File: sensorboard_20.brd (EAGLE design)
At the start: 100 x 58 mm, 107 parts, among them IC1 ECMF02-2AMX6, IC2_ESP32S2WROOMM22S2 ESP32-S2-WROOM_M22S2H3200PH3Q0, IC4 TPA6211A1DRBR, J4_USB USB_CONN, J5_AUDIO SJ-3523-SMT-TR, J6_OAT 2.5mm JACK, J7 30310-6002HB, U1 LPS22HB, U10-MAG_SENSOR MMC5983MA, U11 LDL212PV33R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

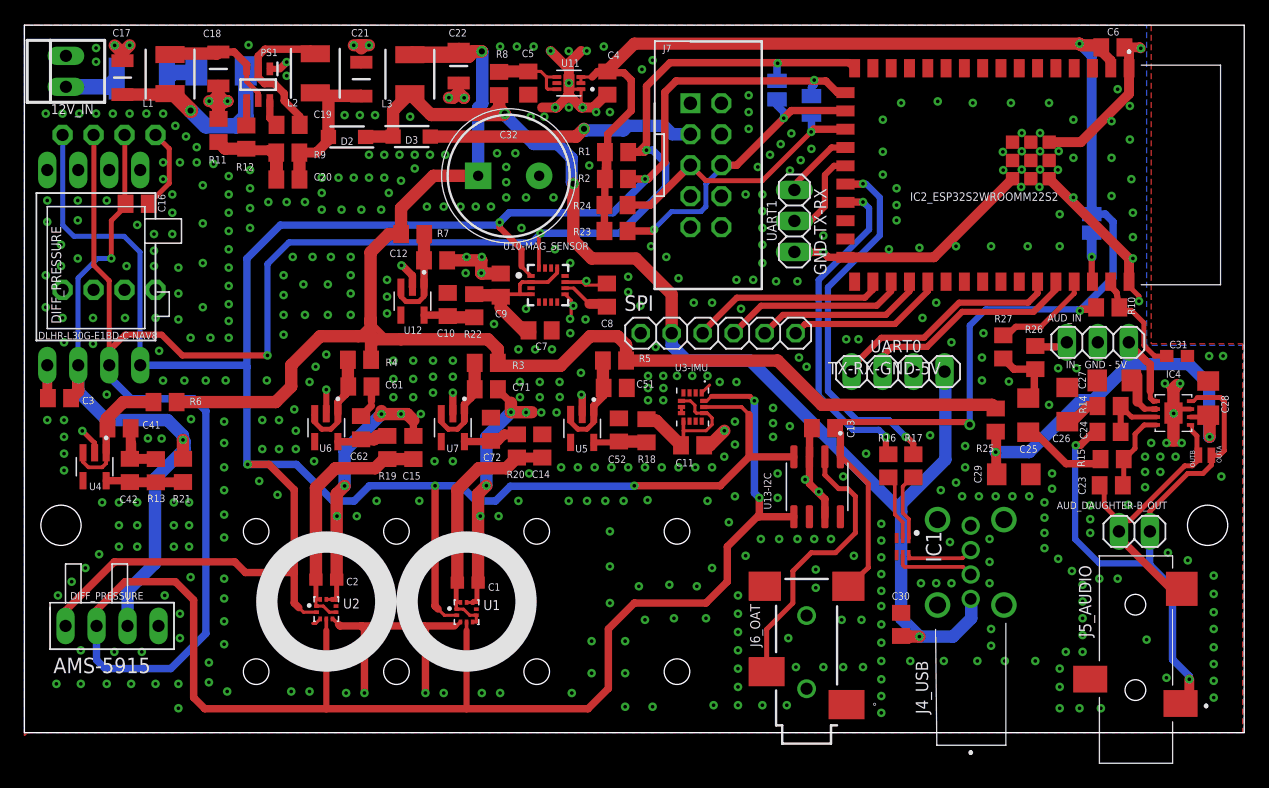
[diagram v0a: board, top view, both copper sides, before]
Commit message: Upload v20 files
Extend UART0 connector with EN, GPIO0 pins (Fixes #2)
Move ESP_AUD, WIFI_EN to different ESP32 pins (Fixes #3)
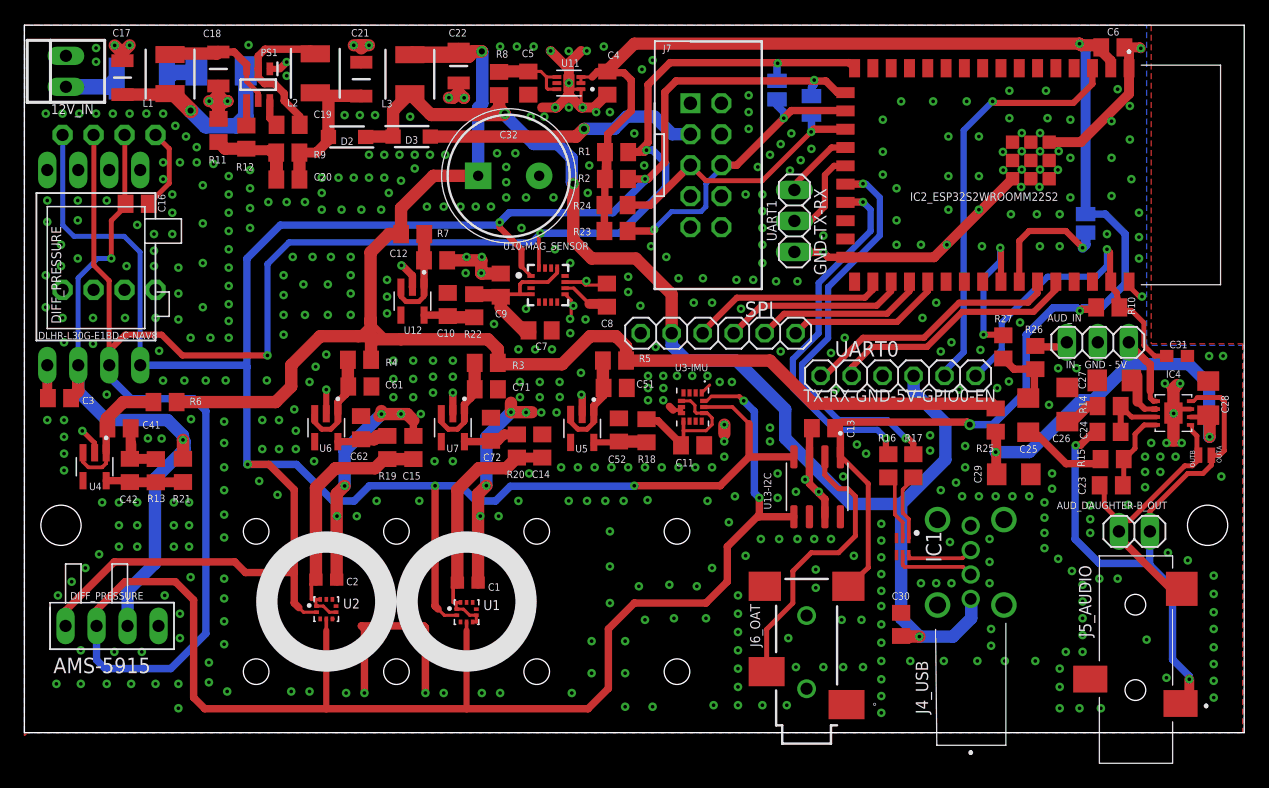
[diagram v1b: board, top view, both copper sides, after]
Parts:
- UART0: device pinhead:1X04 -> pinhead_dD:1X06
- moved WIFI_EN 0.50 mm to (87.0, 41.8)
- moved UART0 0.35 mm to (71.6, 29.2)
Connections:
- removed net N$7: C31.1, IC2_ESP32S2WROOMM22S2.41, R10.1
- new net EN: C31.1, IC2_ESP32S2WROOMM22S2.41, R10.1, UART0.6
- new net GPIO0: IC2_ESP32S2WROOMM22S2.3, UART0.5
- net ESP_AUD: now also IC2_ESP32S2WROOMM22S2.35; no longer IC2_ESP32S2WROOMM22S2.39
- net N$25: now also IC2_ESP32S2WROOMM22S2.36; no longer IC2_ESP32S2WROOMM22S2.40
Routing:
- net GPIO0: track 0.00 -> 34.3 mm, vias 0 -> 1
- net EN: track 0.00 -> 28.9 mm, vias 0 -> 1
- net GND: track 207.2 -> 179.9 mm, vias 554 -> 570
- net N$7: track 8.95 -> 0.00 mm
- net N$25: track 4.28 -> 10.8 mm
- net ESP_AUD: track 8.20 -> 12.5 mm, vias 0 -> 2
- net USB_D+: track 27.7 -> 30.3 mm
- net USB_D-: track 30.6 -> 33.2 mm
- net U0TXD: track 19.1 -> 21.5 mm
- net U0RXD: track 18.4 -> 20.7 mm
- net 5VD: track 110.2 -> 112.0 mm
- net VDD2F: track 20.9 -> 21.4 mm
- net 5V_EXT: track 22.1 -> 22.6 mm
- net SDA0: track 261.9 -> 261.4 mm
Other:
- board text added: "TX-RX-GND-5V-GPIO0-EN"
- board text removed: "TX-RX-GND-5V"
